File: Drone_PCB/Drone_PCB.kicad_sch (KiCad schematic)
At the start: 44 parts, among them J1 Conn_01x04_Pin, J2 Conn_01x04_Pin, J3 Conn_01x04_Pin, J4 Conn_01x06_Pin, J5 Conn_01x06_Pin, J6 USB_B_Micro, Q1 BSS214NW, Q2 BSS214NW, SW2 SW_DPST_x2, U1 STM32F411RCT6, U2 AP2112K-3.3, U3 TP4056-42-ESOP8, U4 DW01A, Y1 26MHz

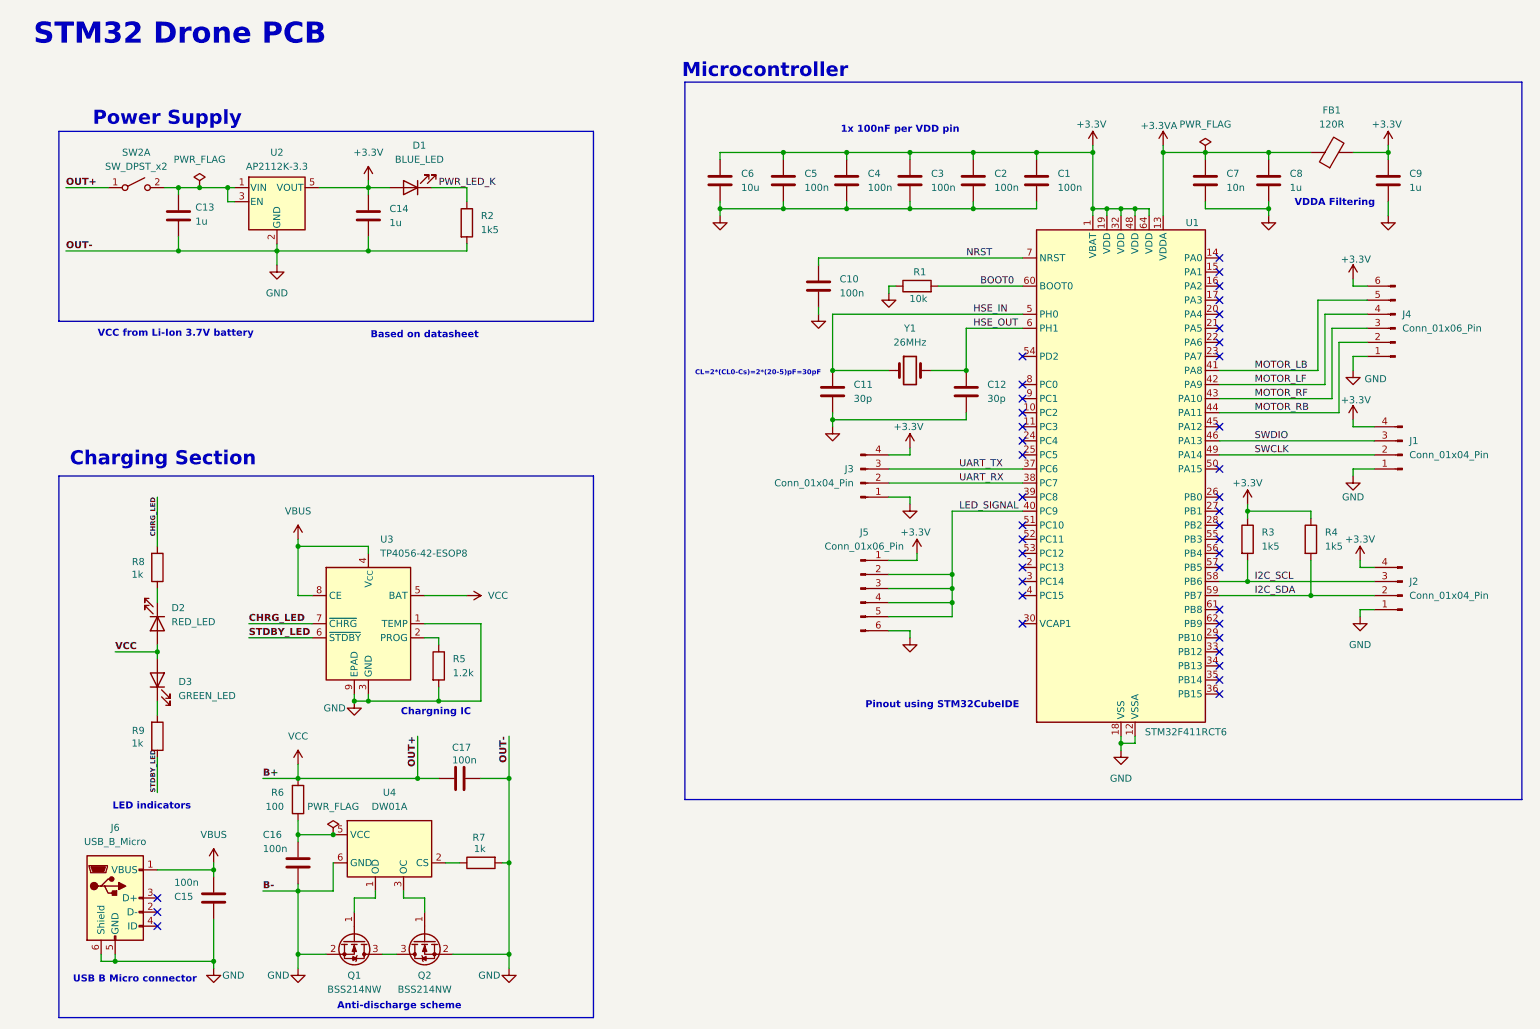
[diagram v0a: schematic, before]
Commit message: Adjusted some pinouts
Corrected pinouts for motors leds and communication modules
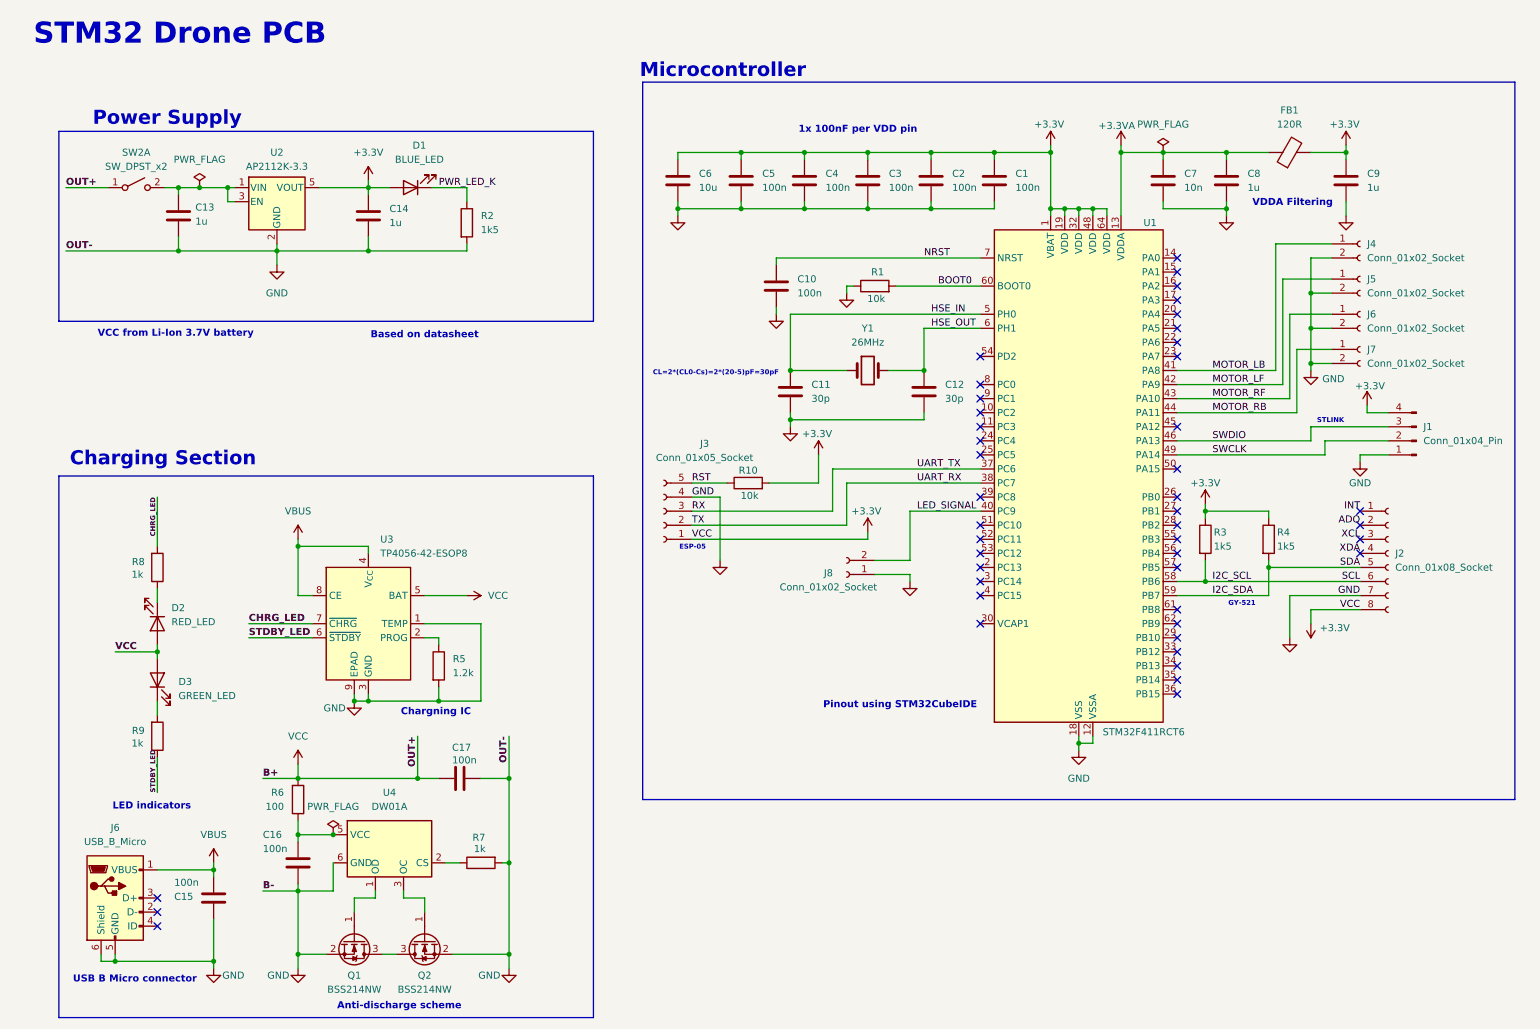
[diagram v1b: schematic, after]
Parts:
- removed J2, J3: Conn_01x04_Pin, Connector_PinHeader_2.54mm:PinHeader_1x04_P2.54mm_Vertical, symbol Connector:Conn_01x04_Pin
- removed J4, J5: Conn_01x06_Pin, Connector_PinHeader_2.54mm:PinHeader_1x06_P2.54mm_Vertical, symbol Connector:Conn_01x06_Pin
- added J2: Conn_01x08_Socket, symbol Connector:Conn_01x08_Socket
- added J3: Conn_01x05_Socket, symbol Connector:Conn_01x05_Socket
- added J4, J5, J6, J7, J8: Conn_01x02_Socket, symbol Connector:Conn_01x02_Socket
- added R10: 10k, Resistor_SMD:R_0402_1005Metric, symbol Device:R
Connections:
- net VCC is gone; now on net +3.3V: C17.1, D2.2 (A), D3.2 (A), R6.2, SW2.1 (A), U3.5 (BAT)
- net +3.3V: now also J2.8 (Pin_8), J3.1 (Pin_1), R10.2
- net GND: now also J2.7 (Pin_7), J3.4 (Pin_4), J4.2 (Pin_2), J5.2 (Pin_2), J6.2 (Pin_2), J7.2 (Pin_2), J8.1 (Pin_1)
- net I2C_SCL: now also J2.6 (Pin_6)
- net I2C_SDA: now also J2.5 (Pin_5)
- net LED_SIGNAL: now also J8.2 (Pin_2)
- net MOTOR_LB: now also J4.1 (Pin_1)
- net MOTOR_LF: now also J5.1 (Pin_1)
- net MOTOR_RB: now also J7.1 (Pin_1)
- net MOTOR_RF: now also J6.1 (Pin_1)
- net UART_RX renamed TX
- net TX: now also J3.2 (Pin_2)
- net UART_TX renamed RX
- net RX: now also J3.3 (Pin_3)
- new net ADO: J2.2 (Pin_2)
- new net INT: J2.1 (Pin_1)
- new net RST: J3.5 (Pin_5), R10.1
- new net XCL: J2.3 (Pin_3)
- new net XDA: J2.4 (Pin_4)
- no-connect marks 41 -> 45
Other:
- note added: "ESP-05"
- note added: "GY-521"
- note added: "STLINK"
- moved on the sheet: C1, C10, C11, C12, C2, C3, C4, C5, C6, C7, C8, C9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

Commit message: Updated motors
We control MOSFETS with PWM so there will not be any overcurrent
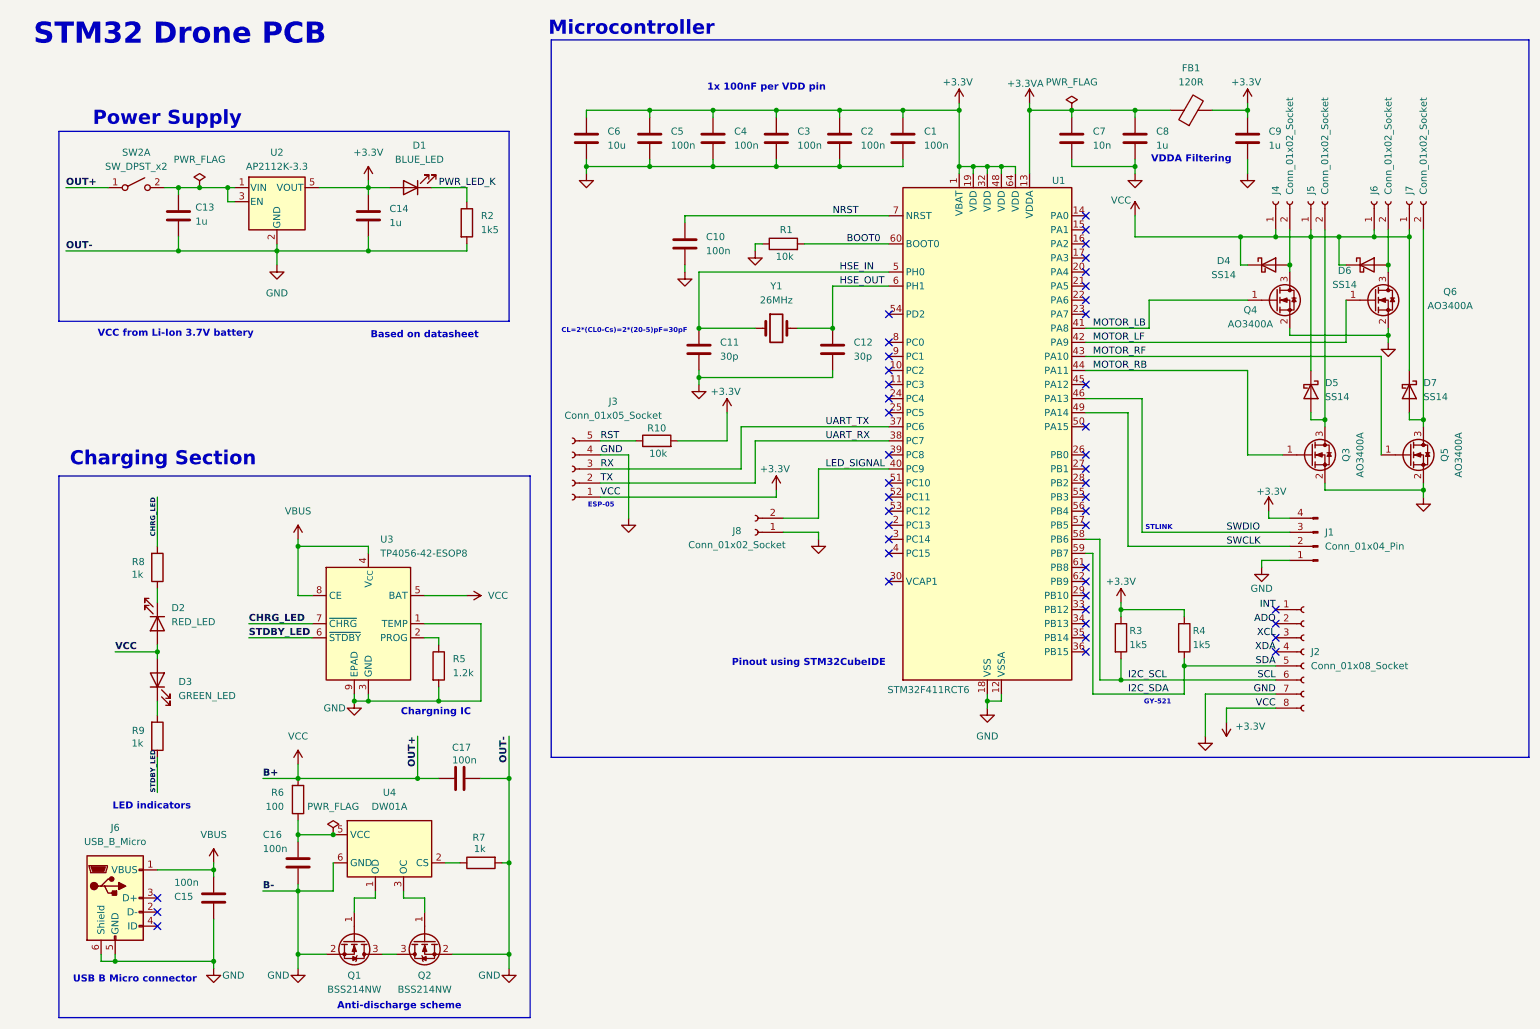
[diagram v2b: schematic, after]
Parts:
- added D4, D5, D6, D7: SS14, Diode_SMD:D_SMA, symbol Diode:SS14
- added Q3, Q4, Q5, Q6: AO3400A, Package_TO_SOT_SMD:SOT-23, symbol Transistor_FET:AO3400A
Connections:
- net +3.3V: now also J4.1 (Pin_1), J5.1 (Pin_1), J6.1 (Pin_1), J7.1 (Pin_1), D4.1 (K), D5.1 (K), D6.1 (K), D7.1 (K)
- net GND: now also Q3.2 (S), Q4.2 (S), Q5.2 (S), Q6.2 (S); no longer J4.2 (Pin_2), J5.2 (Pin_2), J6.2 (Pin_2), J7.2 (Pin_2)
- net MOTOR_LB: now also Q4.1 (G); no longer J4.1 (Pin_1)
- net MOTOR_LF: now also Q6.1 (G); no longer J5.1 (Pin_1)
- net MOTOR_RB: now also Q3.1 (G); no longer J7.1 (Pin_1)
- net MOTOR_RF: now also Q5.1 (G); no longer J6.1 (Pin_1)
- new net: D4.2 (A), J4.2 (Pin_2), Q4.3 (D)
- new net: D7.2 (A), J7.2 (Pin_2), Q5.3 (D)
- new net: D5.2 (A), J5.2 (Pin_2), Q3.3 (D)
- new net: D6.2 (A), J6.2 (Pin_2), Q6.3 (D)
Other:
- moved on the sheet: C1, C10, C11, C12, C2, C3, C4, C5, C6, C7, C8, C9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
